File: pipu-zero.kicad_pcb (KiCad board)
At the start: 4 copper layers, 80 x 50.5 mm, 81 parts, among them IC1 BQ25176JDSGR, J1 USB_C_Receptacle_USB2.0_14P, J2 Conn_01x08, J3 Micro_SD_Card_Det1, Q1 NMOS, Q2 NMOS, Q3 NMOS, Q4 NMOS, SW1 SW_Push, SW2 SW_Push, U1 BQ297xy, U2 MCP1640Bx-xCHY, U3 MCP1727-0802xSN, U4 ESP32-S3-WROOM-1, U5 CC1101, U6 DM-OLED096-636, U7 TSOP348xx, Y2 Crystal_GND23

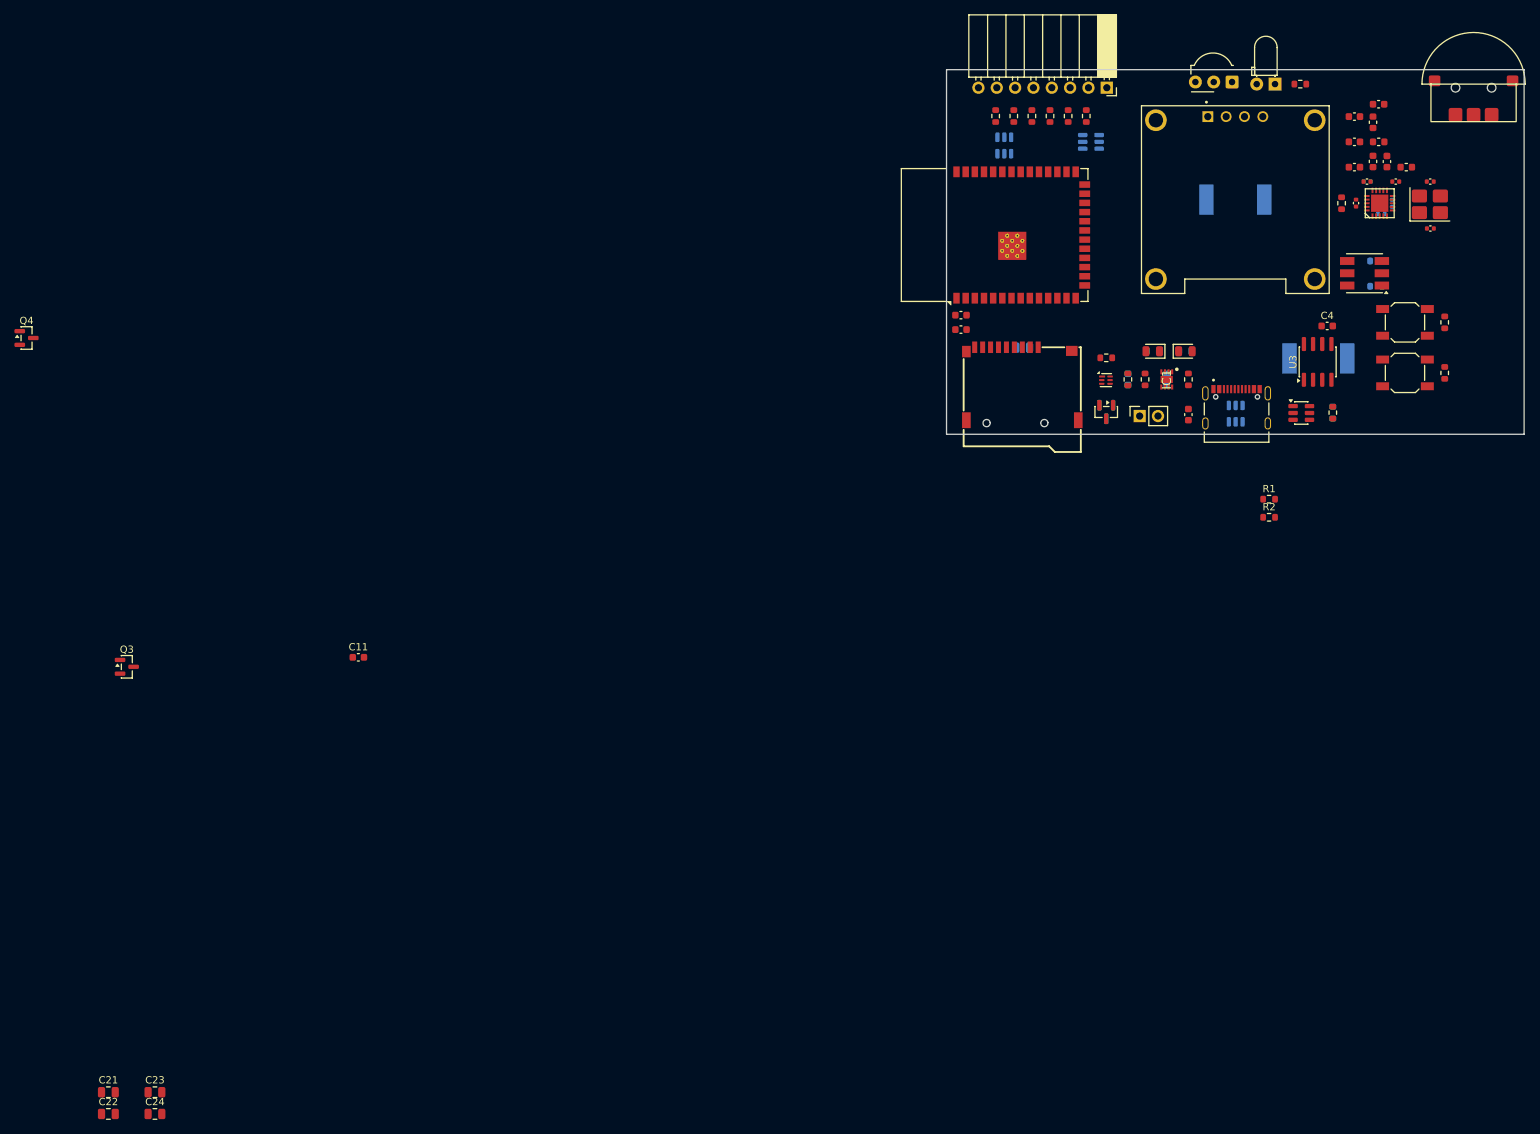
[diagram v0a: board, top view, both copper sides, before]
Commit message: finish component placement on pcb
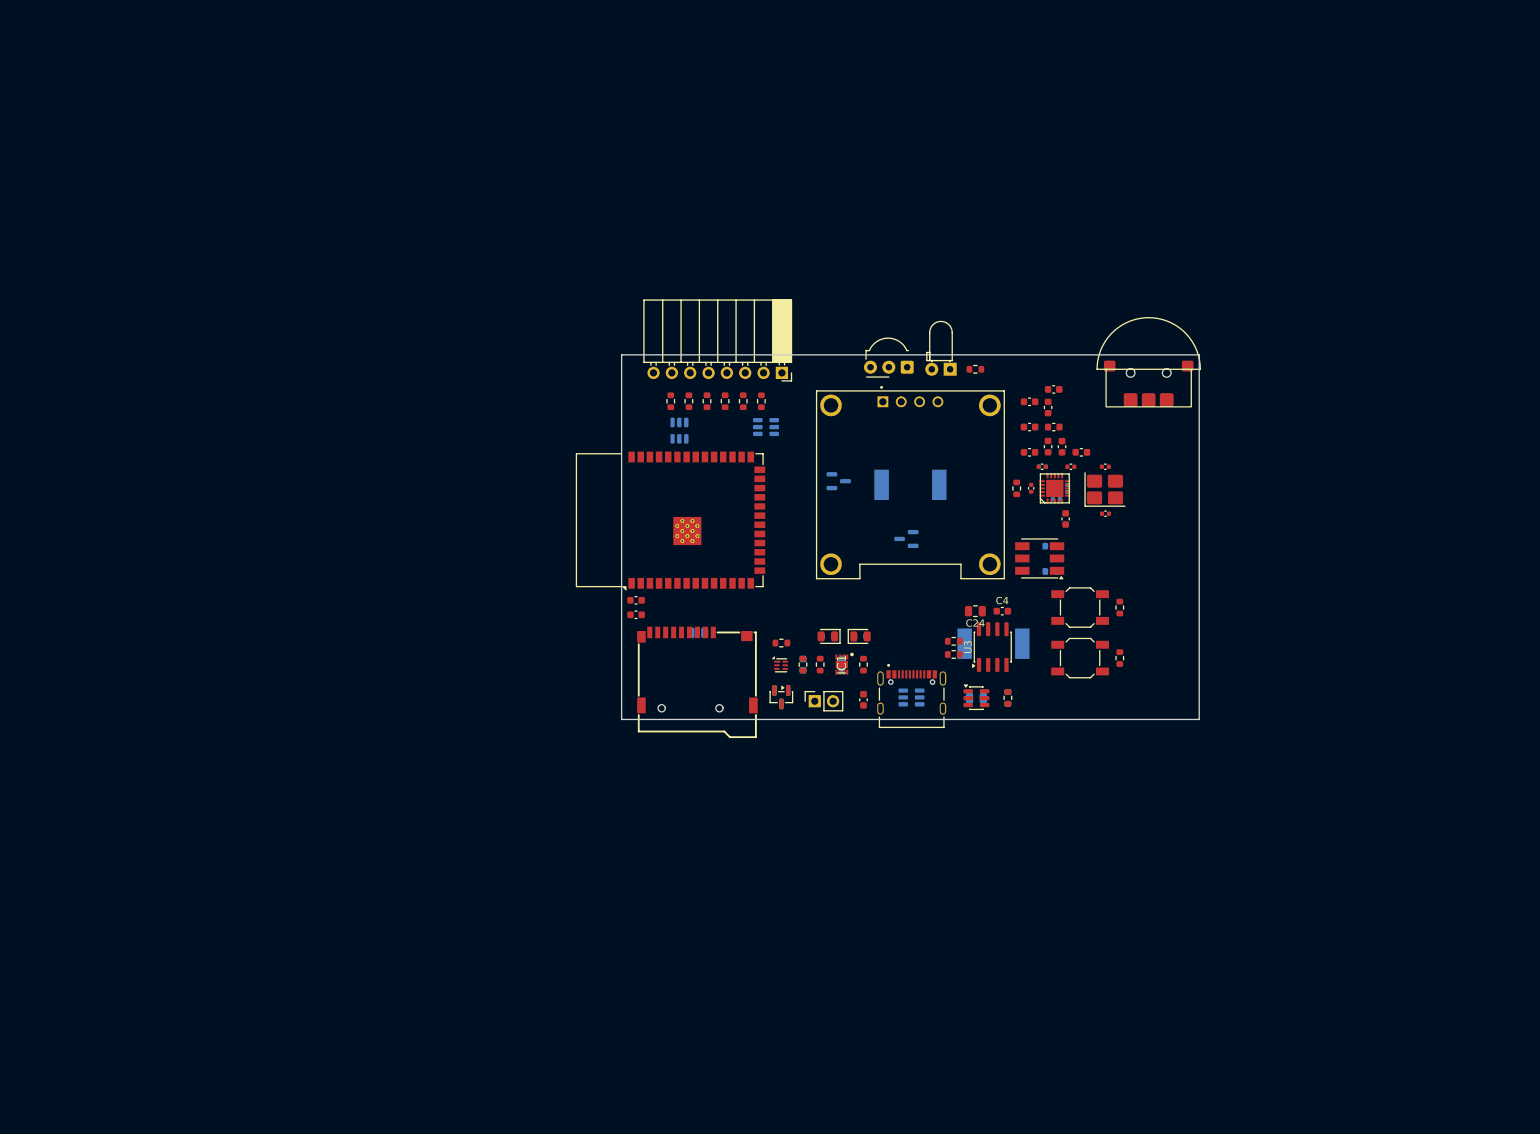
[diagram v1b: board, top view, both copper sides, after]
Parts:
- removed C21, C22: C, Capacitor_SMD:C_0805_2012Metric
- C23, Q3, Q4: moved to B.Cu
- moved C24 133.3 mm to (162.5, 98.0), turned to 180 degrees
- moved C23 126.2 mm to (162.6, 110.0), turned to 180 degrees
- moved Q4 114.2 mm to (143.6, 80.0)
- moved Q3 109.4 mm to (152.9, 88.0), turned to 180 degrees
- moved C11 99.8 mm to (175.0, 85.2), turned to -90 degrees
- moved C25 59.9 mm to (124.0, 101.0)
- moved R16 59.9 mm to (127.8, 68.9)
- moved BT1 59.9 mm to (140.2, 110.5)
- moved BZ1 59.9 mm to (153.5, 80.5)
- moved C1 59.9 mm to (144.0, 105.4)
- moved C10 59.9 mm to (171.8, 78.0)
- moved C12 59.9 mm to (171.7, 78.0)
- moved C13 59.9 mm to (175.2, 81.0)
- moved C14 59.9 mm to (180.5, 84.5)
- moved C15 59.9 mm to (180.5, 78.0)
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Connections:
- D5 pad 1: /I-O/IO39_EXT -> /I-O/IO39
- D5 pad 3: /I-O/IO40_EXT -> /I-O/IO40
- D5 pad 4: /I-O/IO41_EXT -> /I-O/IO41
- D5 pad 6: /I-O/IO42_EXT -> /I-O/IO42
- J1 pad A1: (no net) -> GND
- J1 pad A4: (no net) -> /USB_VBUS

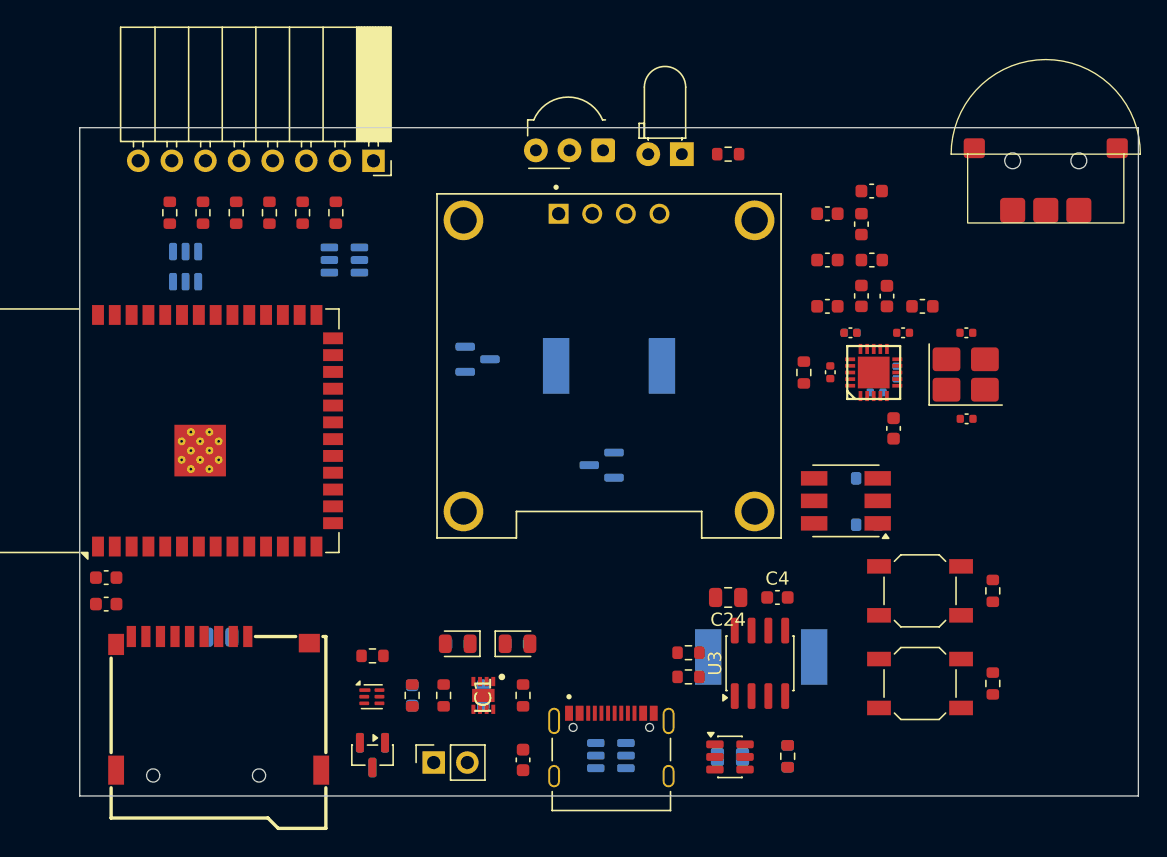
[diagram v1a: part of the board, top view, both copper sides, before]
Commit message: add layer filling
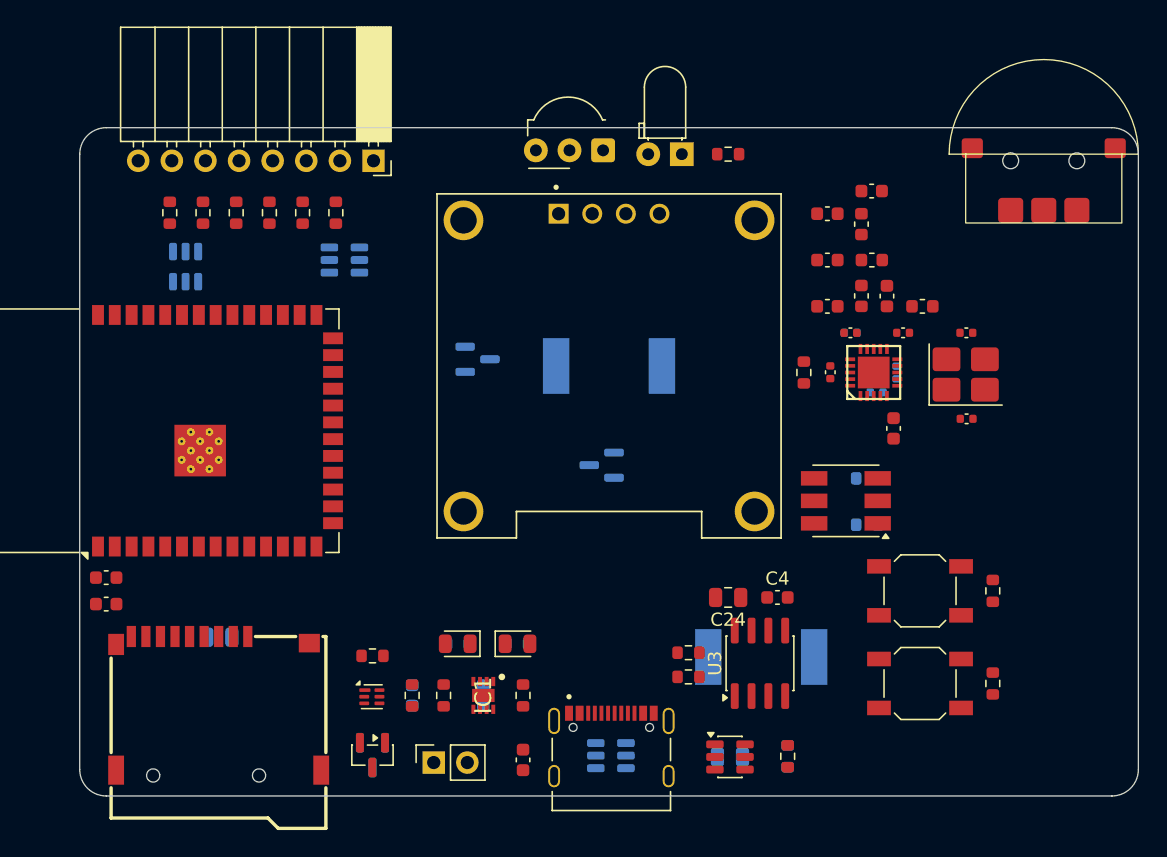
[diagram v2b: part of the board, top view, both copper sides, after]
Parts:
- moved U8 0.15 mm to (186.3, 68.8)
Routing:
- added copper zone on In1.Cu, net +3V3
- added copper zone on In2.Cu, net GND
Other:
- outline, holes or cut-outs redrawn
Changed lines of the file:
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@@
 			(at -4.38 20.55 90)
 			(layer "F.Fab")
+			(hide yes)
 			(effects
 				(font
@@
 	(footprint "Encoder:encoder"
 		(layer "F.Cu")
-		(at 186.5 68.75)
+		(at 186.35 68.75)
 		(property "Reference" "U8"
 			(at 0 7 0)
@@
 		)
 	)
-	(gr_rect
-		(start 113.5 62.5)
-		(end 193.5 113)
+	(gr_arc
+		(start 191.5 62.5)
+		(mid 192.914214 63.085786)
+		(end 193.5 64.5)
+		(stroke
+			(width 0.05)
+			(type default)
+		)
+		(layer "Edge.Cuts")
+	)
+	(gr_arc
+		(start 113.5 64.5)
+		(mid 114.085786 63.085786)
+		(end 115.5 62.5)
+		(stroke
+			(width 0.05)
+			(type default)
+		)
+		(layer "Edge.Cuts")
+	)
+	(gr_arc
+		(start 115.5 113)
+		(mid 114.085786 112.414214)
+		(end 113.5 111)
+		(stroke
+			(width 0.05)
+			(type default)
+		)
+		(layer "Edge.Cuts")
+	)
+	(gr_line
+		(start 191.5 62.5)
+		(end 115.5 62.5)
+		(stroke
+			(width 0.05)
+			(type default)
+		)
+		(layer "Edge.Cuts")
+	)
+	(gr_line
+		(start 113.5 64.5)
+		(end 113.5 111)
+		(stroke
+			(width 0.05)
+			(type default)
+		)
+		(layer "Edge.Cuts")
+	)
+	(gr_line
+		(start 193.5 111)
+		(end 193.5 64.5)
+		(stroke
+			(width 0.05)
+			(type default)
+		)
+		(layer "Edge.Cuts")
+	)
+	(gr_arc
+		(start 193.5 111)
+		(mid 192.914214 112.414214)
+		(end 191.5 113)
 		(stroke
 			(width 0.05)
-			(type solid)
+			(type default)
 		)
-		(fill no)
 		(layer "Edge.Cuts")
 	)
+	(gr_line
+		(start 115.5 113)
+		(end 191.5 113)
+		(stroke
+			(width 0.05)
+			(type default)
+		)
+		(layer "Edge.Cuts")
+	)
+	(zone
+		(net 8)
+		(net_name "+3V3")
+		(layer "In1.Cu")
+		(hatch edge 0.5)
+		(connect_pads
+			(clearance 0.5)
+		)
+		(min_thickness 0.25)
+		(filled_areas_thickness no)
+		(fill
+			(thermal_gap 0.5)
+			(thermal_bridge_width 0.5)
+		)
+		(polygon
+			(pts
+				(xy 111.527834 60.527834) (xy 111.5 115) (xy 196 115) (xy 196 60.5)
+			)
+		)
+	)
+	(zone
+		(net 3)
+		(net_name "GND")
+		(layer "In2.Cu")
+		(hatch edge 0.5)
+		(priority 1)
+		(connect_pads
+			(clearance 0.5)
+		)
+		(min_thickness 0.25)
+		(filled_areas_thickness no)
+		(fill
+			(thermal_gap 0.5)
+			(thermal_bridge_width 0.5)
+		)
+		(polygon
+			(pts
+				(xy 111.527834 60.527834) (xy 196 60.5) (xy 196 115) (xy 111.5 115)
+			)
+		)
+	)
 	(embedded_fonts no)

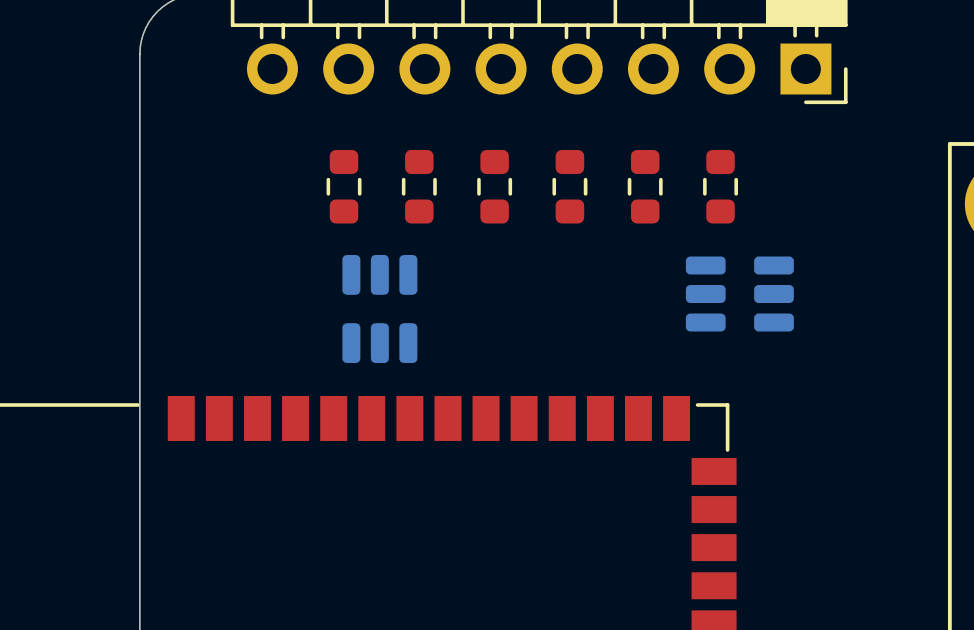
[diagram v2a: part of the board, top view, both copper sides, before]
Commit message: initial component routing
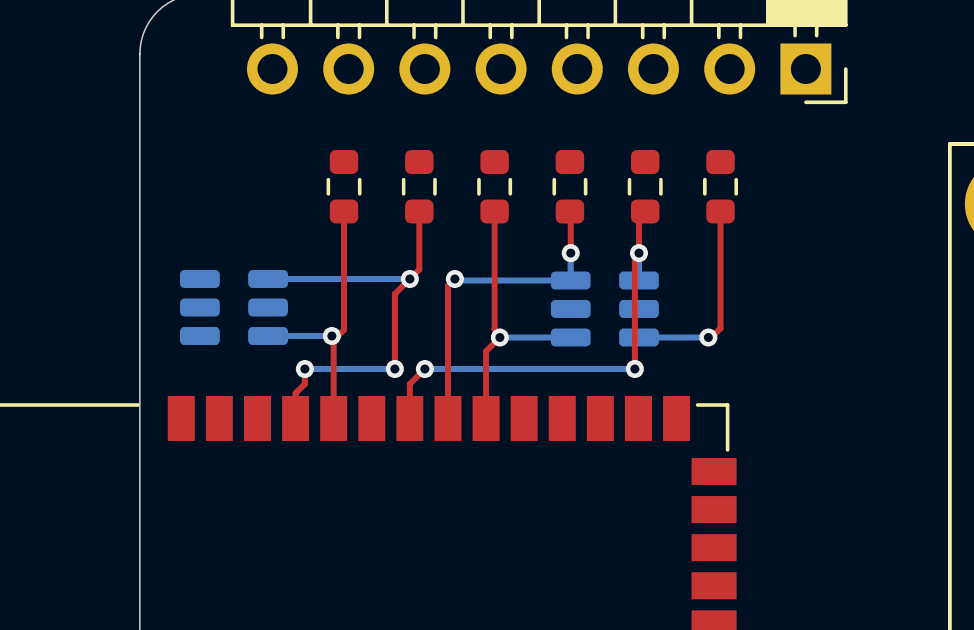
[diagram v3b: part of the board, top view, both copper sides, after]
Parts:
- moved D6 4.86 mm to (116.6, 73.0), turned to 0 degrees
- moved D5 4.53 mm to (129.0, 73.0)
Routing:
- net /I-O/IO41: track 0.00 -> 15.2 mm, vias 0 -> 3
- net /I-O/TXD0: track 0.00 -> 15.1 mm, vias 0 -> 3
- net /I-O/IO40: track 0.00 -> 10.9 mm, vias 0 -> 2
- net /I-O/IO39: track 0.00 -> 9.53 mm, vias 0 -> 1
- net /I-O/RXD0: track 0.00 -> 9.33 mm, vias 0 -> 1
- net /I-O/IO42: track 0.00 -> 6.74 mm, vias 0 -> 1
